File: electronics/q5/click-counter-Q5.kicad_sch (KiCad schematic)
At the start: 0 parts

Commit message: WIP: Q5 design-lock routing iteration snapshot (not verified)
Co-Authored-By: Claude Opus 5.5 <noreply@anthropic.com>
Claude-Session: https://claude.ai/code/session_01UrkzLMrBi6iLPSL5SbMCA7
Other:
- note added: "C39 / C40 / C5 / D1 / D2 / D3"
- note added: "D4 / J1 / R1 / R19 / R2 / R3"
- note added: "Q5 schematic index - 81 fitted PCB parts plus non-fitted test lands and mounts. Global net labels connect the functional sheets. Crosses explicitly mark unused physical pins. Q1 submitted files remain frozen. This candidate still requires ERC, layout, first-article and safety qualification."
- note added: "R30 / R31 / R34 / R35 / R38 / R4"
- note added: "R5 / R6 / TP13 / U2 / U3 / U7"
- note removed: "C39 / C5 / D1 / D2 / D3 / D4"
- note removed: "J1 / R1 / R19 / R2 / R3 / R30"
- note removed: "Q5 schematic index - 79 fitted PCB parts plus non-fitted test lands and mounts. Global net labels connect the functional sheets. Crosses explicitly mark unused physical pins. Q1 submitted files remain frozen. This candidate still requires ERC, layout, first-article and safety qualification."
- note removed: "R31 / R34 / R35 / R4 / R5 / R6"
- note removed: "TP13 / U2 / U3 / U7"
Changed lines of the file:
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@@
  (paper "A3") (title_block (title "Count Fidget - Q5 engineering candidate") (rev "Q5 candidate")
       (company "Count Fidget") (comment 1 "ENGINEERING CANDIDATE - NOT RELEASED FOR MANUFACTURE"))
-(text "Q5 schematic index - 79 fitted PCB parts plus non-fitted test lands and mounts.\nGlobal net labels connect the functional sheets. Crosses explicitly mark unused physical pins.\nQ1 submitted files remain frozen. This candidate still requires ERC, layout, first-article and safety qualification." (at 20 20 0) (effects (font (size 1.27 1.27)) (justify left top)))
+(text "Q5 schematic index - 81 fitted PCB parts plus non-fitted test lands and mounts.\nGlobal net labels connect the functional sheets. Crosses explicitly mark unused physical pins.\nQ1 submitted files remain frozen. This candidate still requires ERC, layout, first-article and safety qualification." (at 20 20 0) (effects (font (size 1.27 1.27)) (justify left top)))
 (sheet (at 14 48) (size 126 28) (stroke (width .254) (type solid))
           (fill (color 0 0 0 0))
@@
           (property "Sheetname" "USB, charging, soft power latch and common supply / 2" (at 210 155.19 0) (effects (font (size 1.016 1.016)))) (property "Sheetfile" "usb-power-2.kicad_sch" (at 210 190.81 0) (effects (font (size 1.016 1.016))))
           (instances (project "click-counter-Q5" (path "/7c190cd8-3ca2-5363-8a92-396d30a08243" (page "12")))))
-(text "C39 / C5 / D1 / D2 / D3 / D4" (at 151 168 0) (effects (font (size 1.016 1.016)) (justify left top)))
+(text "C39 / C40 / C5 / D1 / D2 / D3" (at 151 168 0) (effects (font (size 1.016 1.016)) (justify left top)))
 (sheet (at 280 159) (size 126 28) (stroke (width .254) (type solid))
           (fill (color 0 0 0 0))
           (property "Sheetname" "USB, charging, soft power latch and common supply / 3" (at 343 155.19 0) (effects (font (size 1.016 1.016)))) (property "Sheetfile" "usb-power-3.kicad_sch" (at 343 190.81 0) (effects (font (size 1.016 1.016))))
           (instances (project "click-counter-Q5" (path "/7c190cd8-3ca2-5363-8a92-396d30a08243" (page "13")))))
-(text "J1 / R1 / R19 / R2 / R3 / R30" (at 284 168 0) (effects (font (size 1.016 1.016)) (justify left top)))
+(text "D4 / J1 / R1 / R19 / R2 / R3" (at 284 168 0) (effects (font (size 1.016 1.016)) (justify left top)))
 (sheet (at 14 196) (size 126 28) (stroke (width .254) (type solid))
           (fill (color 0 0 0 0))
           (property "Sheetname" "USB, charging, soft power latch and common supply / 4" (at 77 192.19 0) (effects (font (size 1.016 1.016)))) (property "Sheetfile" "usb-power-4.kicad_sch" (at 77 227.81 0) (effects (font (size 1.016 1.016))))
           (instances (project "click-counter-Q5" (path "/7c190cd8-3ca2-5363-8a92-396d30a08243" (page "14")))))
-(text "R31 / R34 / R35 / R4 / R5 / R6" (at 18 205 0) (effects (font (size 1.016 1.016)) (justify left top)))
+(text "R30 / R31 / R34 / R35 / R38 / R4" (at 18 205 0) (effects (font (size 1.016 1.016)) (justify left top)))
 (sheet (at 147 196) (size 126 28) (stroke (width .254) (type solid))
           (fill (color 0 0 0 0))
           (property "Sheetname" "USB, charging, soft power latch and common supply / 5" (at 210 192.19 0) (effects (font (size 1.016 1.016)))) (property "Sheetfile" "usb-power-5.kicad_sch" (at 210 227.81 0) (effects (font (size 1.016 1.016))))
           (instances (project "click-counter-Q5" (path "/7c190cd8-3ca2-5363-8a92-396d30a08243" (page "15")))))
-(text "TP13 / U2 / U3 / U7" (at 151 205 0) (effects (font (size 1.016 1.016)) (justify left top)))
+(text "R5 / R6 / TP13 / U2 / U3 / U7" (at 151 205 0) (effects (font (size 1.016 1.016)) (justify left top)))
 (sheet (at 280 196) (size 126 28) (stroke (width .254) (type solid))
           (fill (color 0 0 0 0))

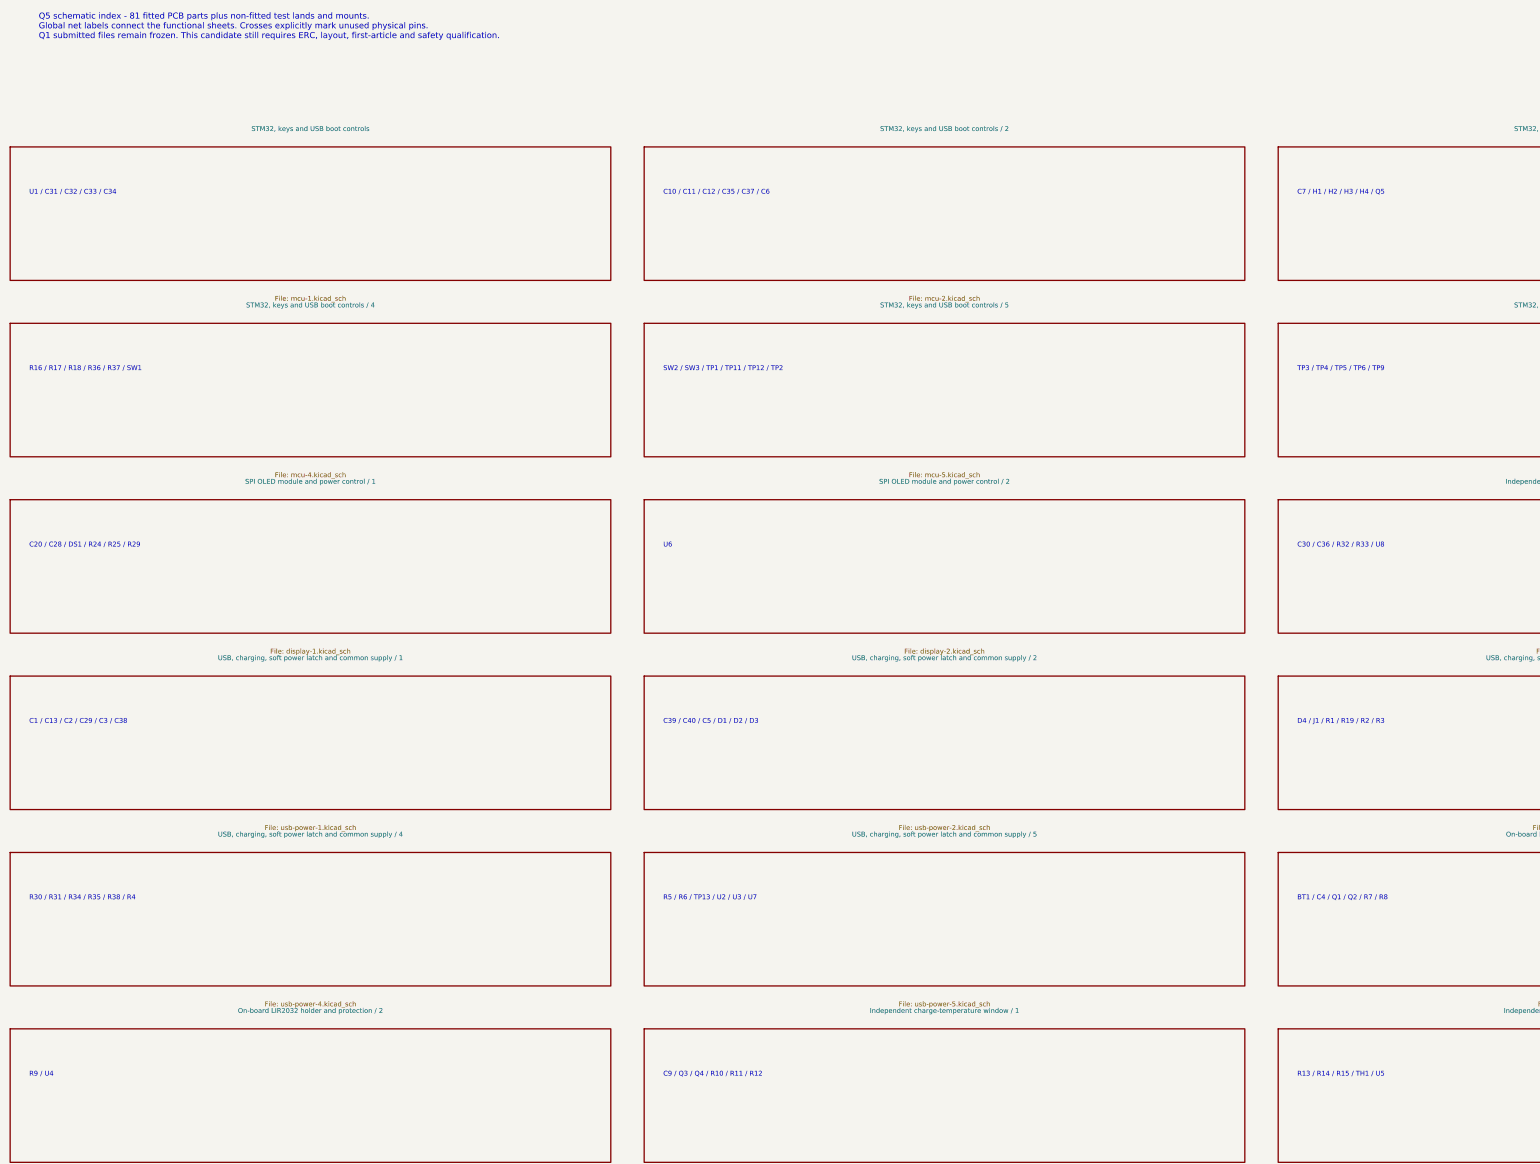
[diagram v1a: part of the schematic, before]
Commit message: First-order de-risking: U5 supply filter, 10 nF latch cap, JLC-corrected CPLs, DFU unplug rule
Three independent checks (datasheet pinouts, JLC EasyEDA footprints, dead-on-arrival
review) found no pinout, footprint or DOA defect. Changes from their findings:
R39 1k + C9 filter U5's 6 V abs-max supply from VBUS hot-plug ringing; C40 10 nF
(min latch press 10.5 ms typ); JLC-corrected CPL files and a preview checklist;
flasher warns to reset a unit left in DFU before unplugging. Board re-routed:
DRC/ERC/parity zero, no via-to-land gaps; emulator 0 failures; stock 43/43.

Co-Authored-By: Claude Opus 5.5 <noreply@anthropic.com>
Claude-Session: https://claude.ai/code/session_01UrkzLMrBi6iLPSL5SbMCA7
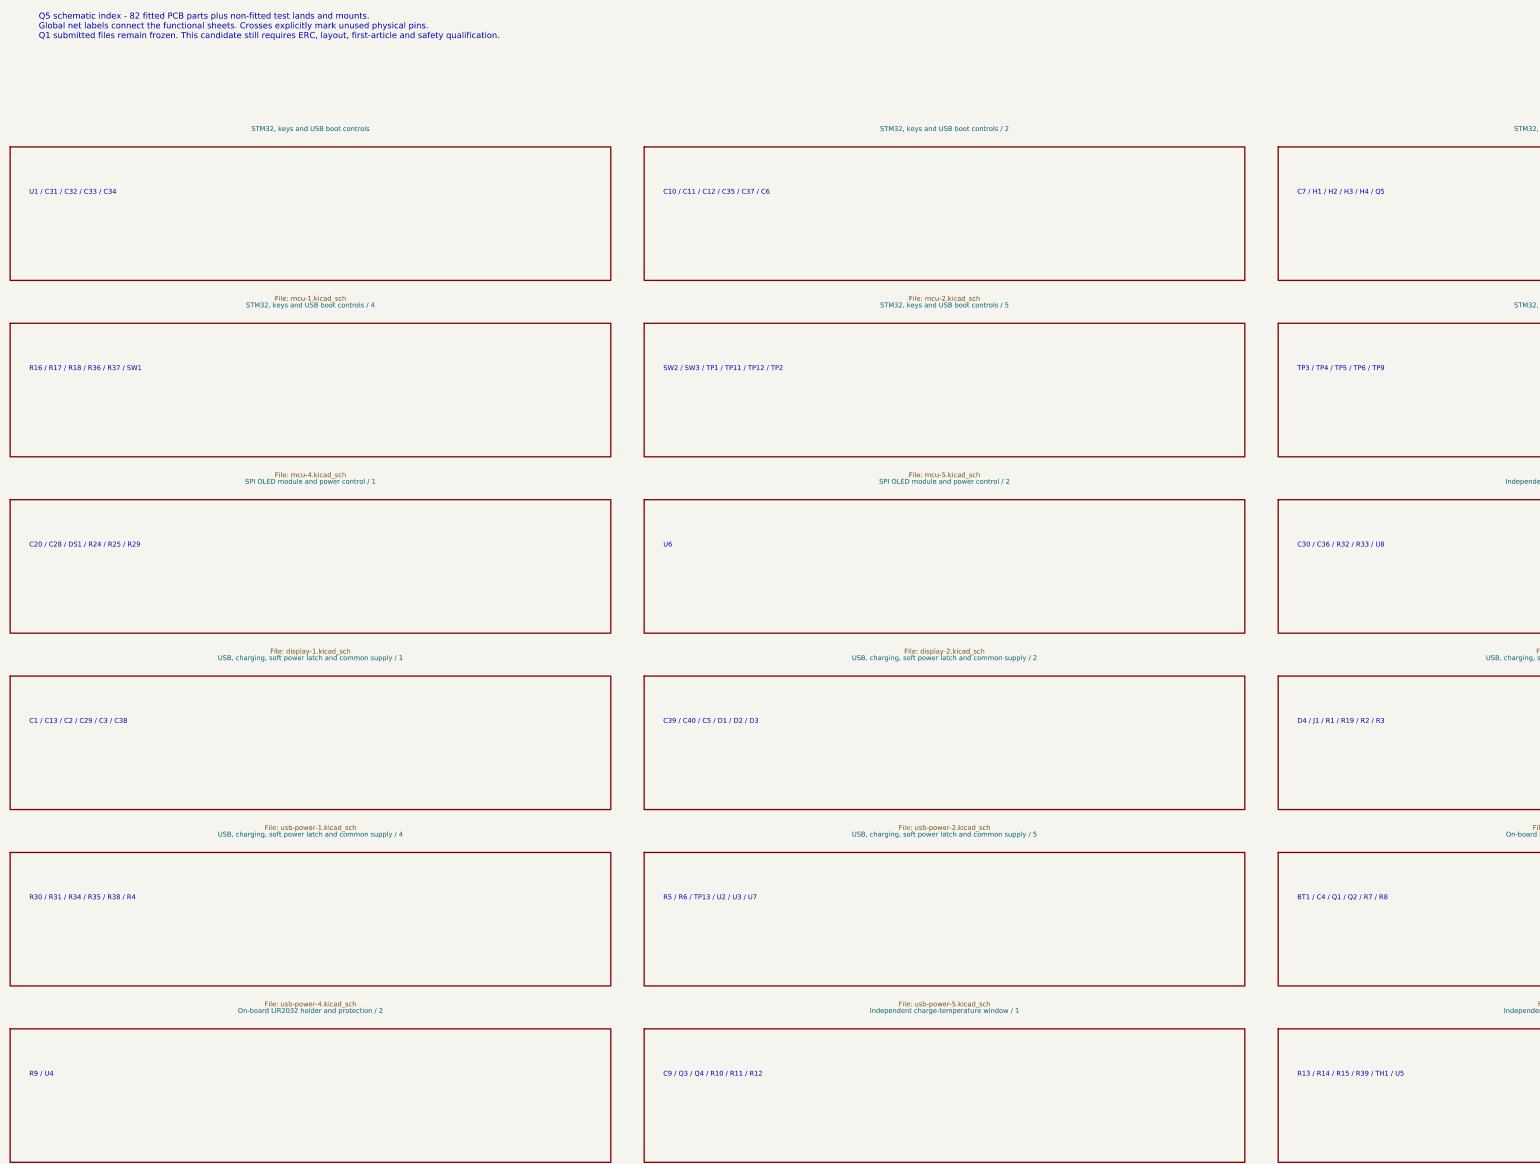
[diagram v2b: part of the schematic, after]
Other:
- note added: "Q5 schematic index - 82 fitted PCB parts plus non-fitted test lands and mounts. Global net labels connect the functional sheets. Crosses explicitly mark unused physical pins. Q1 submitted files remain frozen. This candidate still requires ERC, layout, first-article and safety qualification."
- note added: "R13 / R14 / R15 / R39 / TH1 / U5"
- note removed: "Q5 schematic index - 81 fitted PCB parts plus non-fitted test lands and mounts. Global net labels connect the functional sheets. Crosses explicitly mark unused physical pins. Q1 submitted files remain frozen. This candidate still requires ERC, layout, first-article and safety qualification."
- note removed: "R13 / R14 / R15 / TH1 / U5"
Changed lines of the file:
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@@
  (paper "A3") (title_block (title "Count Fidget - Q5 engineering candidate") (rev "Q5 candidate")
       (company "Count Fidget") (comment 1 "ENGINEERING CANDIDATE - NOT RELEASED FOR MANUFACTURE"))
-(text "Q5 schematic index - 81 fitted PCB parts plus non-fitted test lands and mounts.\nGlobal net labels connect the functional sheets. Crosses explicitly mark unused physical pins.\nQ1 submitted files remain frozen. This candidate still requires ERC, layout, first-article and safety qualification." (at 20 20 0) (effects (font (size 1.27 1.27)) (justify left top)))
+(text "Q5 schematic index - 82 fitted PCB parts plus non-fitted test lands and mounts.\nGlobal net labels connect the functional sheets. Crosses explicitly mark unused physical pins.\nQ1 submitted files remain frozen. This candidate still requires ERC, layout, first-article and safety qualification." (at 20 20 0) (effects (font (size 1.27 1.27)) (justify left top)))
 (sheet (at 14 48) (size 126 28) (stroke (width .254) (type solid))
           (fill (color 0 0 0 0))
@@
           (property "Sheetname" "Independent charge-temperature window / 2" (at 343 229.19 0) (effects (font (size 1.016 1.016)))) (property "Sheetfile" "thermal-2.kicad_sch" (at 343 264.81 0) (effects (font (size 1.016 1.016))))
           (instances (project "click-counter-Q5" (path "/7c190cd8-3ca2-5363-8a92-396d30a08243" (page "19")))))
-(text "R13 / R14 / R15 / TH1 / U5" (at 284 242 0) (effects (font (size 1.016 1.016)) (justify left top)))
+(text "R13 / R14 / R15 / R39 / TH1 / U5" (at 284 242 0) (effects (font (size 1.016 1.016)) (justify left top)))
 (sheet_instances (path "/" (page "1")))
 )
